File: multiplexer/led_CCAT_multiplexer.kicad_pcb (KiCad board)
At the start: 2 copper layers, 101.6 x 50.8 mm, 14 parts, among them J1 Conn_02x12_Top_Bottom, J2 Conn_02x12_Top_Bottom, J3 Conn_02x12_Top_Bottom, J4 Conn_02x12_Top_Bottom, J5 Conn_02x12_Top_Bottom, J6 Conn_02x12_Top_Bottom, J7 Conn_02x12_Top_Bottom, J8 DB25_Female_MountingHoles

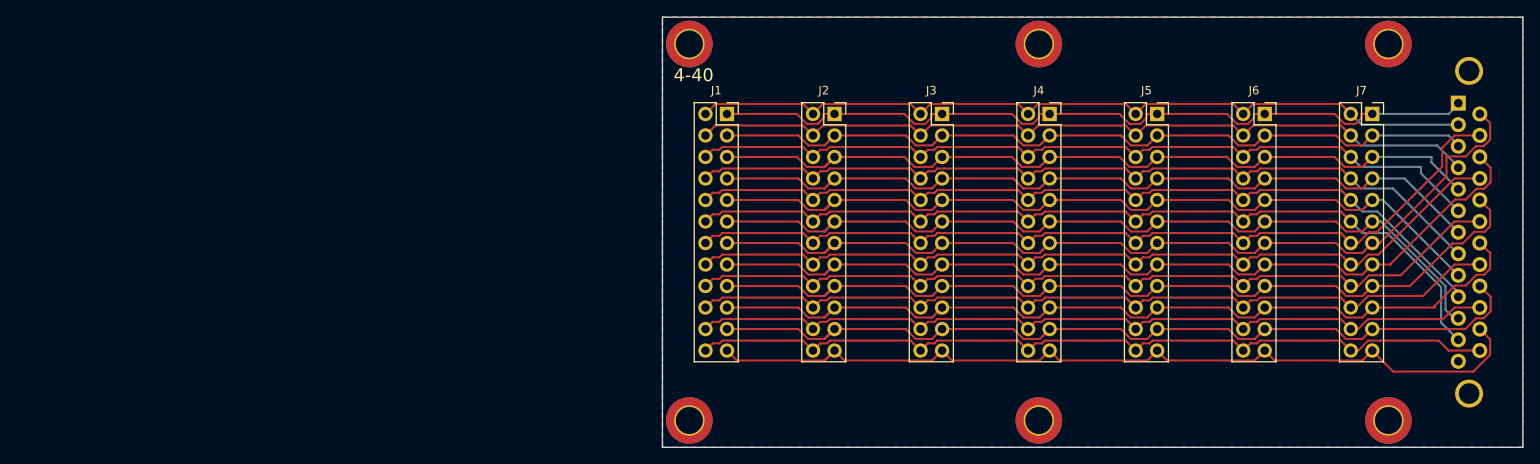
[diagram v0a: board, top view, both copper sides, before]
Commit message: add 6 connectors to multiplexer
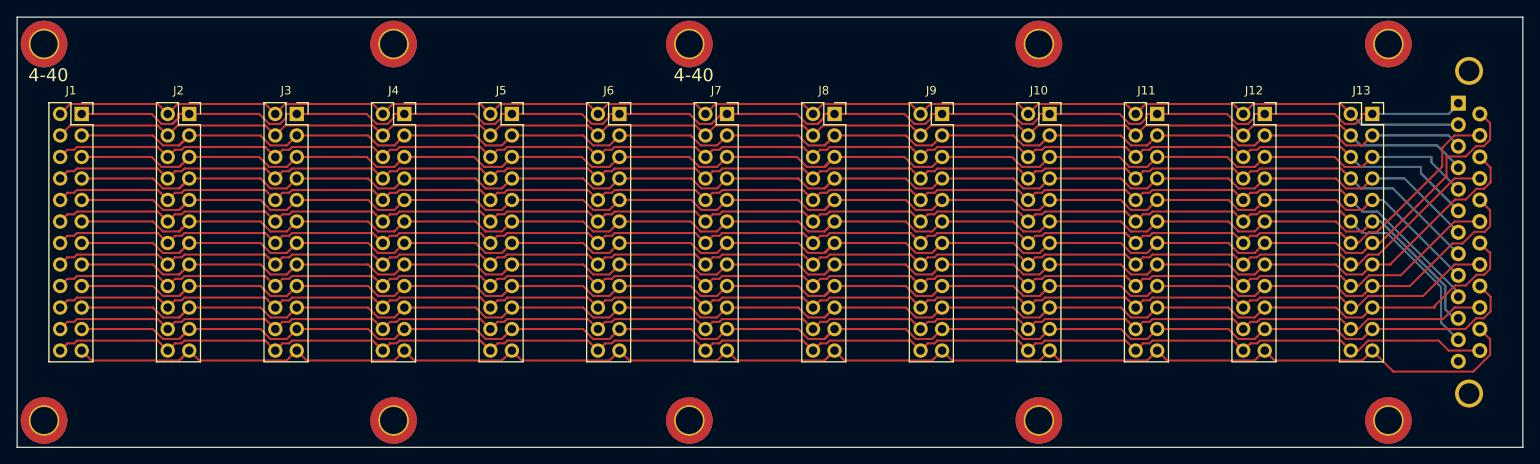
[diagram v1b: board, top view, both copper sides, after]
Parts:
- added J1: Conn_02x12_Top_Bottom, Connector_PinSocket_2.54mm:PinSocket_2x12_P2.54mm_Vertical, F.Cu at (-68.6, 11.4)
- added J2: Conn_02x12_Top_Bottom, Connector_PinSocket_2.54mm:PinSocket_2x12_P2.54mm_Vertical, F.Cu at (-55.9, 11.4)
- added J3: Conn_02x12_Top_Bottom, Connector_PinSocket_2.54mm:PinSocket_2x12_P2.54mm_Vertical, F.Cu at (-43.2, 11.4)
- added J4: Conn_02x12_Top_Bottom, Connector_PinSocket_2.54mm:PinSocket_2x12_P2.54mm_Vertical, F.Cu at (-30.5, 11.4)
- added J5: Conn_02x12_Top_Bottom, Connector_PinSocket_2.54mm:PinSocket_2x12_P2.54mm_Vertical, F.Cu at (-17.8, 11.4)
- added J6: Conn_02x12_Top_Bottom, Connector_PinSocket_2.54mm:PinSocket_2x12_P2.54mm_Vertical, F.Cu at (-5.08, 11.4)
- added REF**: MountingHole_3.2mm_M3_ISO14580_Pad_TopBottom, MountingHole:MountingHole_3.2mm_M3_ISO14580_Pad_TopBottom, F.Cu at (-73.0, 3.17)
- added REF**: MountingHole_3.2mm_M3_ISO14580_Pad_TopBottom, MountingHole:MountingHole_3.2mm_M3_ISO14580_Pad_TopBottom, F.Cu at (-31.8, 47.6)
- added REF**: MountingHole_3.2mm_M3_ISO14580_Pad_TopBottom, MountingHole:MountingHole_3.2mm_M3_ISO14580_Pad_TopBottom, F.Cu at (-31.8, 3.17)
- added REF**: MountingHole_3.2mm_M3_ISO14580_Pad_TopBottom, MountingHole:MountingHole_3.2mm_M3_ISO14580_Pad_TopBottom, F.Cu at (-73.0, 47.6)
- renumbered J4 to J10, J5 to J11, J6 to J12, J7 to J13, J8 to J14, J1 to J7, J2 to J8, J3 to J9
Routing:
- net /pin1: track 97.1 -> 183.2 mm
- net /pin23: track 103.0 -> 186.7 mm
- net /pin21: track 102.1 -> 185.8 mm
- net /pin13: track 107.5 -> 191.2 mm
- net /pin11: track 99.9 -> 183.6 mm
- net /pin3: track 94.5 -> 178.2 mm
- net /pin17: track 104.1 -> 187.8 mm
- net /pin9: track 97.4 -> 181.1 mm
- net /pin15: track 105.2 -> 188.9 mm
- net /pin5: track 95.8 -> 179.5 mm
- net /pin19: track 103.2 -> 186.9 mm
- net /pin7: track 96.5 -> 180.2 mm
- net /pin6: track 97.8 -> 179.9 mm
- net /pin8: track 98.4 -> 180.5 mm
- net /pin18: track 100.6 -> 182.6 mm
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- removed copper zone on B.Cu, net GND
- removed copper zone on F.Cu, net GND
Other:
- board size 101.6 x 50.8 mm -> 177.8 x 50.8 mm
- board text added: "Conn_02x12_Top_Bottom"
- board text added: "MountingHole_3.2mm_M3_ISO14580_Pad_TopBottom"

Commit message: restore copper zones
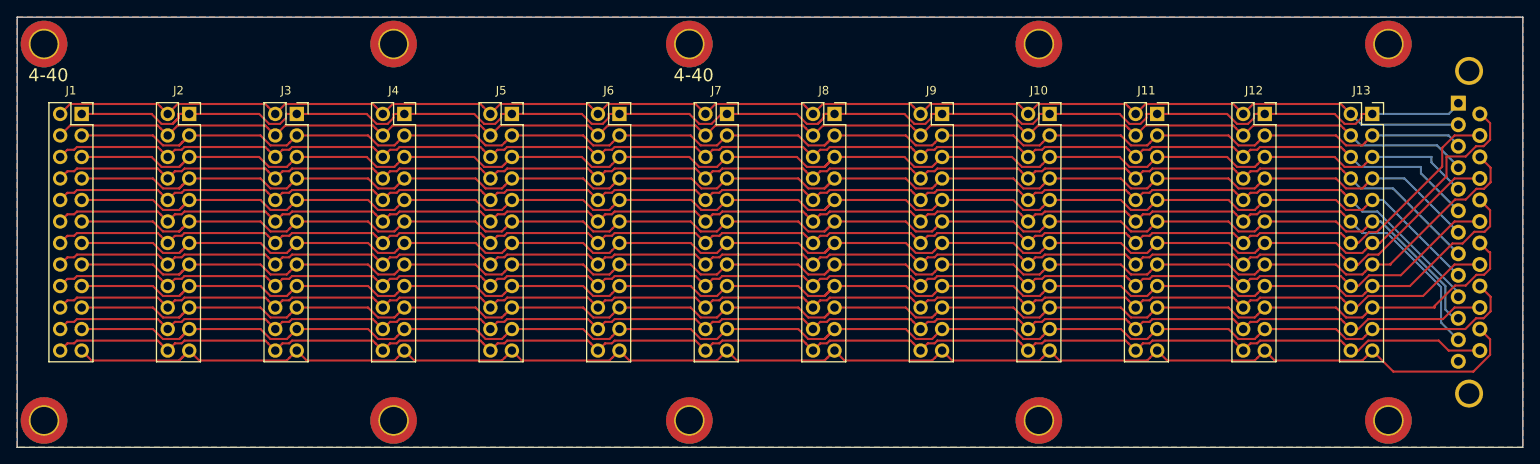
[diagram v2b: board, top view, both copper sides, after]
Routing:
- added copper zone on B.Cu, net GND
- added copper zone on F.Cu, net GND
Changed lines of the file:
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@@
 		(net 24)
 	)
+	(zone
+		(net 25)
+		(net_name "GND")
+		(layer "F.Cu")
+		(hatch edge 0.508)
+		(priority 1)
+		(connect_pads yes
+			(clearance 0.254)
+		)
+		(min_thickness 0.254)
+		(filled_areas_thickness no)
+		(fill yes
+			(thermal_gap 0.254)
+			(thermal_bridge_width 0.508)
+		)
+		(polygon
+			(pts
+				(xy 101.6 50.8) (xy -76.2 50.8) (xy -76.2 0) (xy 101.6 0)
+			)
+		)
+	)
+	(zone
+		(net 25)
+		(net_name "GND")
+		(layer "B.Cu")
+		(hatch edge 0.508)
+		(connect_pads
+			(clearance 0.508)
+		)
+		(min_thickness 0.254)
+		(filled_areas_thickness no)
+		(fill yes
+			(thermal_gap 0.508)
+			(thermal_bridge_width 0.508)
+		)
+		(polygon
+			(pts
+				(xy 101.6 50.8) (xy -76.2 50.8) (xy -76.2 0) (xy 101.6 0)
+			)
+		)
+	)
 )
